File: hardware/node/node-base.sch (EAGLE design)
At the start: 57 parts, among them IC1 HYPERTRIANGLE_TCS3472FN, Q1 32.768kHz, Q2 24MHz, Q3 BS250, U1 INA322_DGK_8, U2 LMV551_DBV_5, X1 BU-SMA-V

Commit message: NODEHW: Routeing rethought, bettered
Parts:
- C14, C15, C6, C7, C8, C9: device SparkFun-Capacitors:CAP0805 -> SparkFun-Capacitors:CAPPTH
- L1: device resistor:L-EU0207/10 -> resistor:L-EU0204/7
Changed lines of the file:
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@@
 <grid distance="0.1" unitdist="inch" unit="inch" style="lines" multiple="1" display="no" altdistance="0.01" altunitdist="inch" altunit="inch"/>
 <layers>
-<layer number="1" name="Top" color="4" fill="1" visible="no" active="no"/>
-<layer number="2" name="Route2" color="1" fill="3" visible="no" active="no"/>
-<layer number="3" name="Route3" color="4" fill="3" visible="no" active="no"/>
-<layer number="4" name="Route4" color="1" fill="4" visible="no" active="no"/>
-<layer number="5" name="Route5" color="4" fill="4" visible="no" active="no"/>
-<layer number="6" name="Route6" color="1" fill="8" visible="no" active="no"/>
-<layer number="7" name="Route7" color="4" fill="8" visible="no" active="no"/>
-<layer number="8" name="Route8" color="1" fill="2" visible="no" active="no"/>
-<layer number="9" name="Route9" color="4" fill="2" visible="no" active="no"/>
-<layer number="10" name="Route10" color="1" fill="7" visible="no" active="no"/>
-<layer number="11" name="Route11" color="4" fill="7" visible="no" active="no"/>
-<layer number="12" name="Route12" color="1" fill="5" visible="no" active="no"/>
-<layer number="13" name="Route13" color="4" fill="5" visible="no" active="no"/>
-<layer number="14" name="Route14" color="1" fill="6" visible="no" active="no"/>
-<layer number="15" name="Route15" color="4" fill="6" visible="no" active="no"/>
-<layer number="16" name="Bottom" color="1" fill="1" visible="no" active="no"/>
-<layer number="17" name="Pads" color="2" fill="1" visible="no" active="no"/>
-<layer number="18" name="Vias" color="2" fill="1" visible="no" active="no"/>
-<layer number="19" name="Unrouted" color="6" fill="1" visible="no" active="no"/>
-<layer number="20" name="Dimension" color="15" fill="1" visible="no" active="no"/>
-<layer number="21" name="tPlace" color="7" fill="1" visible="no" active="no"/>
-<layer number="22" name="bPlace" color="7" fill="1" visible="no" active="no"/>
-<layer number="23" name="tOrigins" color="15" fill="1" visible="no" active="no"/>
-<layer number="24" name="bOrigins" color="15" fill="1" visible="no" active="no"/>
-<layer number="25" name="tNames" color="7" fill="1" visible="no" active="no"/>
-<layer number="26" name="bNames" color="7" fill="1" visible="no" active="no"/>
-<layer number="27" name="tValues" color="7" fill="1" visible="no" active="no"/>
-<layer number="28" name="bValues" color="7" fill="1" visible="no" active="no"/>
+<layer number="1" name="Top" color="4" fill="1" visible="yes" active="no"/>
+<layer number="2" name="Route2" color="1" fill="3" visible="yes" active="no"/>
+<layer number="3" name="Route3" color="4" fill="3" visible="yes" active="no"/>
+<layer number="4" name="Route4" color="1" fill="4" visible="yes" active="no"/>
+<layer number="5" name="Route5" color="4" fill="4" visible="yes" active="no"/>
+<layer number="6" name="Route6" color="1" fill="8" visible="yes" active="no"/>
+<layer number="7" name="Route7" color="4" fill="8" visible="yes" active="no"/>
+<layer number="8" name="Route8" color="1" fill="2" visible="yes" active="no"/>
+<layer number="9" name="Route9" color="4" fill="2" visible="yes" active="no"/>
+<layer number="10" name="Route10" color="1" fill="7" visible="yes" active="no"/>
+<layer number="11" name="Route11" color="4" fill="7" visible="yes" active="no"/>
+<layer number="12" name="Route12" color="1" fill="5" visible="yes" active="no"/>
+<layer number="13" name="Route13" color="4" fill="5" visible="yes" active="no"/>
+<layer number="14" name="Route14" color="1" fill="6" visible="yes" active="no"/>
+<layer number="15" name="Route15" color="4" fill="6" visible="yes" active="no"/>
+<layer number="16" name="Bottom" color="1" fill="1" visible="yes" active="no"/>
+<layer number="17" name="Pads" color="2" fill="1" visible="yes" active="no"/>
+<layer number="18" name="Vias" color="2" fill="1" visible="yes" active="no"/>
+<layer number="19" name="Unrouted" color="6" fill="1" visible="yes" active="no"/>
+<layer number="20" name="Dimension" color="15" fill="1" visible="yes" active="no"/>
+<layer number="21" name="tPlace" color="7" fill="1" visible="yes" active="no"/>
+<layer number="22" name="bPlace" color="7" fill="1" visible="yes" active="no"/>
+<layer number="23" name="tOrigins" color="15" fill="1" visible="yes" active="no"/>
+<layer number="24" name="bOrigins" color="15" fill="1" visible="yes" active="no"/>
+<layer number="25" name="tNames" color="7" fill="1" visible="yes" active="no"/>
+<layer number="26" name="bNames" color="7" fill="1" visible="yes" active="no"/>
+<layer number="27" name="tValues" color="7" fill="1" visible="yes" active="no"/>
+<layer number="28" name="bValues" color="7" fill="1" visible="yes" active="no"/>
 <layer number="29" name="tStop" color="7" fill="3" visible="no" active="no"/>
 <layer number="30" name="bStop" color="7" fill="6" visible="no" active="no"/>
@@
 <layer number="35" name="tGlue" color="7" fill="4" visible="no" active="no"/>
 <layer number="36" name="bGlue" color="7" fill="5" visible="no" active="no"/>
-<layer number="37" name="tTest" color="7" fill="1" visible="no" active="no"/>
-<layer number="38" name="bTest" color="7" fill="1" visible="no" active="no"/>
+<layer number="37" name="tTest" color="7" fill="1" visible="yes" active="no"/>
+<layer number="38" name="bTest" color="7" fill="1" visible="yes" active="no"/>
 <layer number="39" name="tKeepout" color="4" fill="11" visible="no" active="no"/>
 <layer number="40" name="bKeepout" color="1" fill="11" visible="no" active="no"/>
@@
 <layer number="44" name="Drills" color="7" fill="1" visible="no" active="no"/>
 <layer number="45" name="Holes" color="7" fill="1" visible="no" active="no"/>
-<layer number="46" name="Milling" color="3" fill="1" visible="no" active="no"/>
-<layer number="47" name="Measures" color="7" fill="1" visible="no" active="no"/>
-<layer number="48" name="Document" color="7" fill="1" visible="no" active="no"/>
-<layer number="49" name="Reference" color="7" fill="1" visible="no" active="no"/>
-<layer number="50" name="dxf" color="7" fill="1" visible="no" active="no"/>
-<layer number="51" name="tDocu" color="7" fill="1" visible="no" active="no"/>
-<layer number="52" name="bDocu" color="7" fill="1" visible="no" active="no"/>
-<layer number="53" name="tGND_GNDA" color="7" fill="9" visible="no" active="no"/>
-<layer number="54" name="bGND_GNDA" color="1" fill="9" visible="no" active="no"/>
-<layer number="56" name="wert" color="7" fill="1" visible="no" active="no"/>
-<layer number="57" name="tCAD" color="7" fill="1" visible="no" active="no"/>
+<layer number="46" name="Milling" color="3" fill="1" visible="yes" active="no"/>
+<layer number="47" name="Measures" color="7" fill="1" visible="yes" active="no"/>
+<layer number="48" name="Document" color="7" fill="1" visible="yes" active="no"/>
+<layer number="49" name="Reference" color="7" fill="1" visible="yes" active="no"/>
+<layer number="50" name="dxf" color="7" fill="1" visible="yes" active="no"/>
+<layer number="51" name="tDocu" color="7" fill="1" visible="yes" active="no"/>
+<layer number="52" name="bDocu" color="7" fill="1" visible="yes" active="no"/>
+<layer number="53" name="tGND_GNDA" color="7" fill="9" visible="yes" active="no"/>
+<layer number="54" name="bGND_GNDA" color="1" fill="9" visible="yes" active="no"/>
+<layer number="56" name="wert" color="7" fill="1" visible="yes" active="no"/>
+<layer number="57" name="tCAD" color="7" fill="1" visible="yes" active="no"/>
 <layer number="90" name="Modules" color="5" fill="1" visible="yes" active="yes"/>
 <layer number="91" name="Nets" color="2" fill="1" visible="yes" active="yes"/>
@@
 <part name="+3V3" library="supply1" deviceset="+3V3" device=""/>
 <part name="GND4" library="supply1" deviceset="GND" device=""/>
-<part name="C6" library="SparkFun-Capacitors" deviceset="CAP" device="0805" value="100n"/>
-<part name="C7" library="SparkFun-Capacitors" deviceset="CAP" device="0805" value="100n"/>
-<part name="C8" library="SparkFun-Capacitors" deviceset="CAP" device="0805" value="100n"/>
-<part name="C9" library="SparkFun-Capacitors" deviceset="CAP" device="0805" value="100n"/>
+<part name="C6" library="SparkFun-Capacitors" deviceset="CAP" device="PTH" value="100n"/>
+<part name="C7" library="SparkFun-Capacitors" deviceset="CAP" device="PTH" value="100n"/>
+<part name="C8" library="SparkFun-Capacitors" deviceset="CAP" device="PTH" value="100n"/>
+<part name="C9" library="SparkFun-Capacitors" deviceset="CAP" device="PTH" value="100n"/>
 <part name="C10" library="SparkFun-Capacitors" deviceset="CAP_POL" device="PTH2" value="10u"/>
 <part name="+3V4" library="supply1" deviceset="+3V3" device=""/>
@@
 <part name="GND7" library="supply1" deviceset="GND" device=""/>
 <part name="GND8" library="supply1" deviceset="GND" device=""/>
-<part name="C14" library="SparkFun-Capacitors" deviceset="CAP" device="0805" value="7p5"/>
-<part name="C15" library="SparkFun-Capacitors" deviceset="CAP" device="0805" value="7p5"/>
+<part name="C14" library="SparkFun-Capacitors" deviceset="CAP" device="PTH" value="7p5"/>
+<part name="C15" library="SparkFun-Capacitors" deviceset="CAP" device="PTH" value="7p5"/>
 <part name="C16" library="SparkFun-Capacitors" deviceset="CAP" device="PTH" value="7p5"/>
 <part name="C17" library="SparkFun-Capacitors" deviceset="CAP" device="PTH" value="7p5"/>
@@
 <part name="R15" library="resistor" deviceset="R-EU_" device="0204/7" value="220"/>
 <part name="U$4" library="FullyCustom" deviceset="TPS61291" device="DRV"/>
-<part name="L1" library="resistor" deviceset="L-EU" device="0207/10"/>
+<part name="L1" library="resistor" deviceset="L-EU" device="0204/7"/>
 <part name="C12" library="SparkFun-Capacitors" deviceset="CAP" device="PTH" value="10n"/>
 <part name="C13" library="SparkFun-Capacitors" deviceset="CAP" device="PTH" value="10n"/>

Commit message: NODEHW: NODE ROUTING FINISHED!!! YAYYYY!
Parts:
- removed C11: 10n, SparkFun-Capacitors:CAPPTH
- removed R12: 1M, resistor:R-EU_0204/7
- removed S1(DNF)1: SPSTPTH_EZ, SparkFun-Electromechanical:SPSTPTH_EZ
- added PWRCONN: (no value), pinhead:PINHD-1X2
- C7: device SparkFun-Capacitors:CAPPTH -> SparkFun-Capacitors:CAPPTH1
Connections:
- removed net LED_SWITCH: C11.1, R12.1, S1(DNF)1.2, U$2G$4.PE10
- net +3V3: no longer R12.2
- net DETECT_OUT: now also U$2G$3.PC2; no longer U$2G$3.PC0
- net DETECT_REF: now also U$2G$3.PC3; no longer U$2G$3.PC1
- net EXT_PWRUP: now also U$2G$2.PA0; no longer U$2G$3.PC8, U$2G$4.PE11
- net GND: now also PWRCONN.2; no longer C11.2, S1(DNF)1.1
- net RADIO_CS: now also U$2G$3.PC4; no longer U$2G$3.PC14
- net RADIO_INT: now also U$2G$2.PA2; no longer U$2G$2.PB11
- net RADIO_MISO: now also U$2G$3.PC1; no longer U$2G$3.PD6
- net RADIO_MOSI: now also U$2G$3.PC0; no longer U$2G$3.PD7
- net SW_ADDR_1: now also U$2G$3.PC14; no longer U$2G$2.PA10
- net SW_ADDR_2: now also U$2G$3.PC13; no longer U$2G$2.PA9
- net SW_ADDR_3: now also U$2G$3.PC11; no longer U$2G$2.PA8
- net SW_ADDR_4: now also U$2G$3.PC10; no longer U$2G$2.PA2
- net SW_ADDR_5: now also U$2G$3.PC9; no longer U$2G$2.PA1
- net SW_ADDR_6: now also U$2G$3.PC8; no longer U$2G$2.PA0
- net SW_ADDR_7: now also U$2G$3.PD7; no longer U$2G$3.PC11
- net SW_ADDR_8: now also U$2G$3.PD6; no longer U$2G$3.PC13
- net V+: now also PWRCONN.1
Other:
- note removed: "CHECK PC8 doesn't do anything else"
- moved on the sheet: C19, CON_EXTSENSOR, U$2G$2, U$2G$3, X1

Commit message: NODEHW: PSU layout now looks like TI's
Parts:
- L1: device resistor:L-EU0204/7 -> resistor:L-EU0204V
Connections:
- net N$4 renamed VREG_SW
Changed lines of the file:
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@@
 <part name="R15" library="resistor" deviceset="R-EU_" device="0204/7" value="220"/>
 <part name="U$4" library="FullyCustom" deviceset="TPS61291" device="DRV"/>
-<part name="L1" library="resistor" deviceset="L-EU" device="0204/7"/>
+<part name="L1" library="resistor" deviceset="L-EU" device="0204V"/>
 <part name="C12" library="SparkFun-Capacitors" deviceset="CAP" device="PTH" value="10n"/>
 <part name="C13" library="SparkFun-Capacitors" deviceset="CAP" device="PTH" value="10n"/>
@@
 </segment>
 </net>
-<net name="N$4" class="0">
+<net name="VREG_SW" class="0">
 <segment>
 <pinref part="U$4" gate="G$1" pin="SW"/>

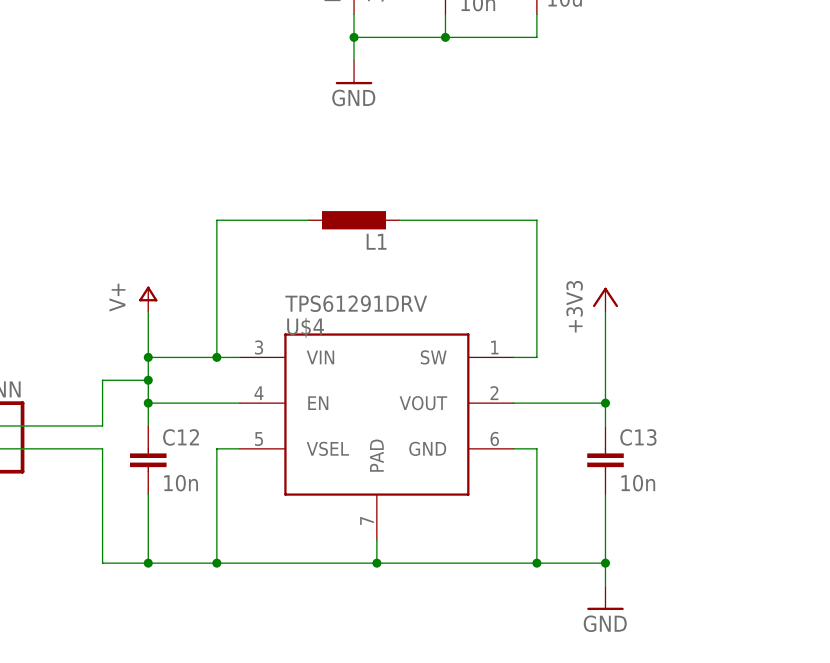
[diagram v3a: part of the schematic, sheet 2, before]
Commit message: NODEHW: New inductor
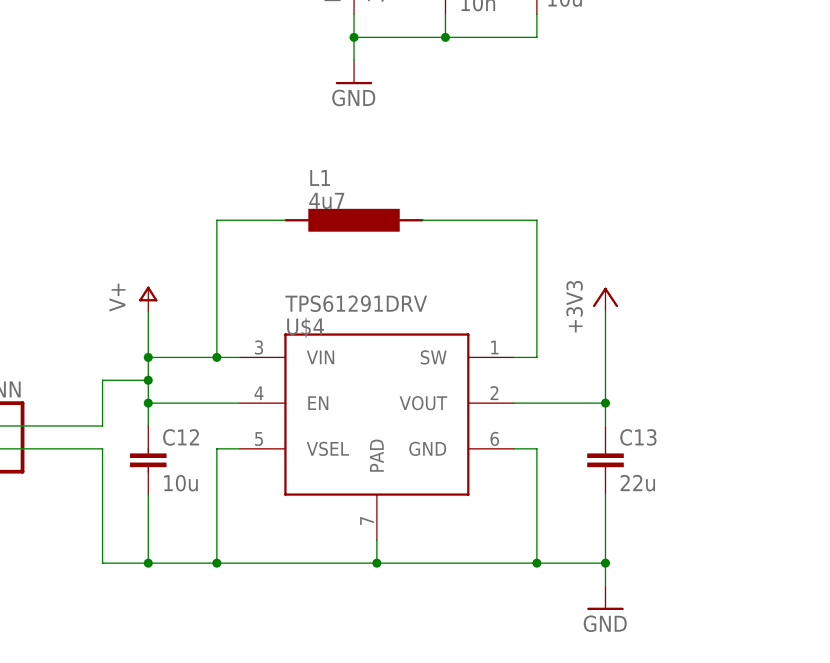
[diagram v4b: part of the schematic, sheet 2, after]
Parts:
- C12: value 10n -> 10u
- C13: value 10n -> 22u
- L1: value (none) -> 4u7; device resistor:L-EU0204V -> FullyCustom:LTF5022
- X1: value BU-SMA-V -> BU-SMA-1-7HOLE; device con-coax:BU-SMA-V -> FullyCustom:BU-SMA-1-7HOLE
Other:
- moved on the sheet: L1
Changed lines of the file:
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@@
 <part name="GND12" library="supply1" deviceset="GND" device=""/>
 <part name="C19" library="SparkFun-Capacitors" deviceset="CAP" device="PTH" value="100n"/>
-<part name="X1" library="con-coax" deviceset="BU-SMA-V" device=""/>
+<part name="X1" library="FullyCustom" deviceset="BU-SMA-1-7HOLE" device=""/>
 <part name="CON_EXTSENSOR" library="pinhead" deviceset="PINHD-1X4" device=""/>
 <part name="GND11" library="supply1" deviceset="GND" device=""/>
@@
 <part name="R15" library="resistor" deviceset="R-EU_" device="0204/7" value="220"/>
 <part name="U$4" library="FullyCustom" deviceset="TPS61291" device="DRV"/>
-<part name="L1" library="resistor" deviceset="L-EU" device="0204V"/>
-<part name="C12" library="SparkFun-Capacitors" deviceset="CAP" device="PTH" value="10n"/>
-<part name="C13" library="SparkFun-Capacitors" deviceset="CAP" device="PTH" value="10n"/>
+<part name="L1" library="FullyCustom" deviceset="LTF5022" device="" value="4u7"/>
+<part name="C12" library="SparkFun-Capacitors" deviceset="CAP" device="PTH" value="10u"/>
+<part name="C13" library="SparkFun-Capacitors" deviceset="CAP" device="PTH" value="22u"/>
 <part name="+3V9" library="supply1" deviceset="+3V3" device=""/>
 <part name="GND15" library="supply1" deviceset="GND" device=""/>
@@
 <instance part="R15" gate="G$1" x="93.98" y="38.1" rot="R90"/>
 <instance part="U$4" gate="G$1" x="180.34" y="63.5"/>
-<instance part="L1" gate="G$1" x="193.04" y="78.74" rot="R90"/>
+<instance part="L1" gate="G$1" x="193.04" y="78.74"/>
 <instance part="C12" gate="G$1" x="170.18" y="50.8"/>
 <instance part="C13" gate="G$1" x="220.98" y="50.8"/>
@@
 <wire x1="177.8" y1="63.5" x2="177.8" y2="78.74" width="0.1524" layer="91"/>
 <junction x="177.8" y="63.5"/>
-<pinref part="L1" gate="G$1" pin="1"/>
-<wire x1="177.8" y1="78.74" x2="187.96" y2="78.74" width="0.1524" layer="91"/>
 <pinref part="U$4" gate="G$1" pin="EN"/>
 <wire x1="180.34" y1="58.42" x2="170.18" y2="58.42" width="0.1524" layer="91"/>
@@
 <wire x1="165.1" y1="60.96" x2="170.18" y2="60.96" width="0.1524" layer="91"/>
 <junction x="170.18" y="60.96"/>
+<pinref part="L1" gate="G$1" pin="1"/>
+<wire x1="177.8" y1="78.74" x2="185.42" y2="78.74" width="0.1524" layer="91"/>
 </segment>
 </net>
@@
 <wire x1="213.36" y1="63.5" x2="213.36" y2="78.74" width="0.1524" layer="91"/>
 <pinref part="L1" gate="G$1" pin="2"/>
-<wire x1="213.36" y1="78.74" x2="198.12" y2="78.74" width="0.1524" layer="91"/>
-</segment>
-</net>
+<wire x1="213.36" y1="78.74" x2="200.66" y2="78.74" width="0.1524" layer="91"/>
+</segment>
+</net>

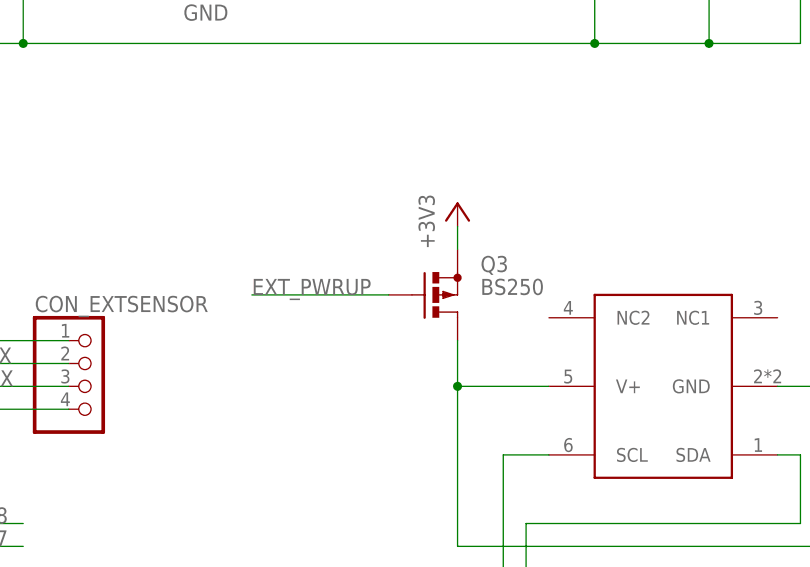
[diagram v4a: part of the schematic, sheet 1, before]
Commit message: NODEHW: Changed transistor package, changed caps to SMD
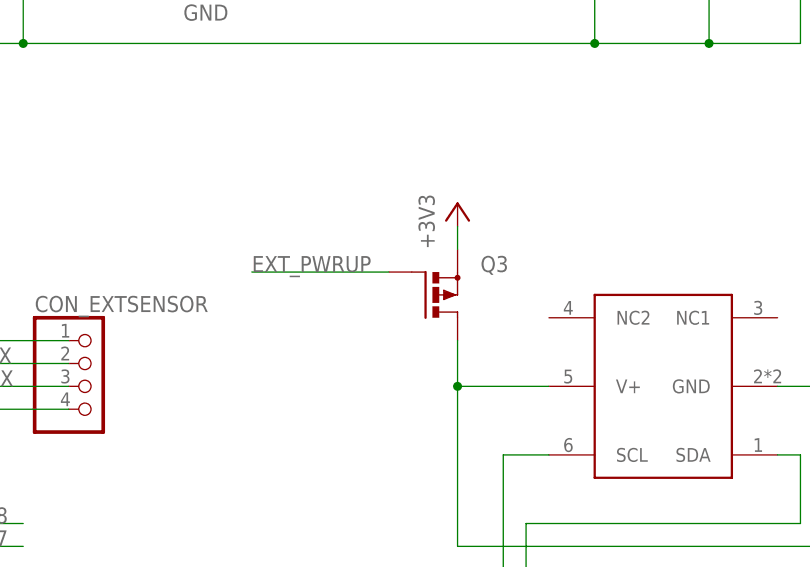
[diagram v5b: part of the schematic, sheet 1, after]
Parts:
- C12, C13: device SparkFun-Capacitors:CAPPTH -> SparkFun-Capacitors:CAP1206
- Q3: value BS250 -> (none); device transistor-small-signal:BS250 -> transistor-power:PMOSFET_PTO220BH
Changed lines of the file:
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@@
 <part name="GND13" library="supply1" deviceset="GND" device=""/>
 <part name="IC1" library="lightsensor" deviceset="HYPERTRIANGLE_TCS3472" device="FN"/>
-<part name="Q3" library="transistor-small-signal" deviceset="BS250" device=""/>
+<part name="Q3" library="transistor-power" deviceset="PMOSFET_P" device="TO220BH"/>
 <part name="FRAME2" library="frames" deviceset="A4L-LOC" device=""/>
 <part name="FRAME1" library="frames" deviceset="A4L-LOC" device=""/>
@@
 <part name="U$4" library="FullyCustom" deviceset="TPS61291" device="DRV"/>
 <part name="L1" library="FullyCustom" deviceset="LTF5022" device="" value="4u7"/>
-<part name="C12" library="SparkFun-Capacitors" deviceset="CAP" device="PTH" value="10u"/>
-<part name="C13" library="SparkFun-Capacitors" deviceset="CAP" device="PTH" value="22u"/>
+<part name="C12" library="SparkFun-Capacitors" deviceset="CAP" device="1206" value="10u"/>
+<part name="C13" library="SparkFun-Capacitors" deviceset="CAP" device="1206" value="22u"/>
 <part name="+3V9" library="supply1" deviceset="+3V3" device=""/>
 <part name="GND15" library="supply1" deviceset="GND" device=""/>
@@
 <instance part="GND13" gate="1" x="238.76" y="40.64"/>
 <instance part="IC1" gate="G$1" x="215.9" y="53.34" rot="MR0"/>
-<instance part="Q3" gate="1" x="187.96" y="88.9"/>
+<instance part="Q3" gate="G$1" x="187.96" y="88.9"/>
 <instance part="FRAME1" gate="G$1" x="0" y="0"/>
 <instance part="SW1" gate="A" x="119.38" y="25.4"/>
@@
 </segment>
 <segment>
-<pinref part="Q3" gate="1" pin="S"/>
+<pinref part="Q3" gate="G$1" pin="S"/>
 <pinref part="+3V7" gate="G$1" pin="+3V3"/>
 <wire x1="190.5" y1="93.98" x2="190.5" y2="96.52" width="0.1524" layer="91"/>
@@
 <wire x1="231.14" y1="60.96" x2="190.5" y2="60.96" width="0.1524" layer="91"/>
 <wire x1="190.5" y1="60.96" x2="190.5" y2="78.74" width="0.1524" layer="91"/>
-<pinref part="Q3" gate="1" pin="D"/>
+<pinref part="Q3" gate="G$1" pin="D"/>
 <wire x1="190.5" y1="78.74" x2="190.5" y2="83.82" width="0.1524" layer="91"/>
 <junction x="190.5" y="78.74"/>
@@
 <net name="EXT_PWRUP" class="0">
 <segment>
-<pinref part="Q3" gate="1" pin="G"/>
-<wire x1="182.88" y1="88.9" x2="167.64" y2="88.9" width="0.1524" layer="91"/>
-<label x="167.64" y="88.9" size="1.778" layer="95"/>
-</segment>
-<segment>
+<pinref part="Q3" gate="G$1" pin="G"/>
+<wire x1="182.88" y1="91.44" x2="167.64" y2="91.44" width="0.1524" layer="91"/>
+<label x="167.64" y="91.44" size="1.778" layer="95"/>
+</segment>
+<segment>
